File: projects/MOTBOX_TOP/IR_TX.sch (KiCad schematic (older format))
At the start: 2 parts, among them J14 Conn_01x02

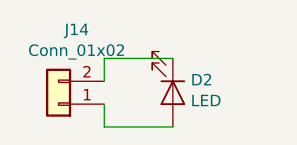
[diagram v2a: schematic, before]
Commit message: New library files and schematics with ESE31 and DT045 switches
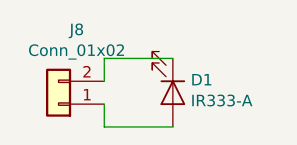
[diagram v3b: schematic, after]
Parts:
- D1: renamed from D2; value LED -> IR333-A
- renumbered J14 to J8
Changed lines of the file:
@@
 EESchema Schematic File Version 4
-LIBS:MOTBOX_TOP-cache
+LIBS:MOTBOX_TOP_ESE31-cache
 EELAYER 26 0
 EELAYER END
@@
 $EndDescr
 $Comp
-L Device:LED D2
+L Device:LED D1
 U 1 1 5CC072E3
 P 4850 2800
-F 0 "D2" V 4795 2878 50  0000 L CNN
-F 1 "LED" V 4886 2878 50  0000 L CNN
+F 0 "D1" V 4795 2878 50  0000 L CNN
+F 1 "IR333-A" V 4886 2878 50  0000 L CNN
 F 2 "LED_THT:LED_D5.0mm_Horizontal_O6.35mm_Z9.0mm" H 4850 2800 50  0001 C CNN
 F 3 "~" H 4850 2800 50  0001 C CNN
@@
 	4550 2650 4850 2650
 $Comp
-L Connector_Generic:Conn_01x02 J14
+L Connector_Generic:Conn_01x02 J8
 U 1 1 5CC2835A
 P 4350 2850
-F 0 "J14" H 4270 2525 50  0000 C CNN
+F 0 "J8" H 4270 2525 50  0000 C CNN
 F 1 "Conn_01x02" H 4270 2616 50  0000 C CNN
 F 2 "Connector_Wire:SolderWirePad_1x02_P3.81mm_Drill0.8mm" H 4350 2850 50  0001 C CNN
